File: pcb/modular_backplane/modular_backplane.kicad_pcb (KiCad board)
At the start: 2 copper layers, 63.5 x 114.3 mm, 50 parts, among them U1 DMP3028LK3-13, U2 DMP3028LK3-13, U3 PREC002SAAN-RC, U4 NTD4969NT4G, U5 PREC002SAAN-RC, U6 NTD4969NT4G

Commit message: updates
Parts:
- added R15: 10K, Resistor_SMD:R_1206_3216Metric_Pad1.42x1.75mm_HandSolder, F.Cu at (45.9, 48.4)
- added R16: 10K, Resistor_SMD:R_1206_3216Metric_Pad1.42x1.75mm_HandSolder, F.Cu at (50.9, 48.4)
- added i2cPins1: PREC002SAAN-RC, backplane:PREC002SAAN-RC, F.Cu at (40.8, 47.5)
- boardToCard1, boardToCard2, boardToCard3, boardToCard4, boardToCard5, boardToCard6, boardToCard7, boardToCard8, boardToCard9: value SSQ-104-02-T-S-RA -> SSQ-108-02-T-S-RA; footprint backplane:SSQ-104-02-T-S-RA -> backplane:SSQ-108-02-T-S-RA
- moved boardToCard9 38.4 mm to (63.5, 50.8)
- moved LipoGnd2 14.0 mm to (54.6, 120.7)
- moved lipoGnd1 14.0 mm to (24.1, 120.7)
- moved lipoIn1 14.0 mm to (8.89, 120.7)
- moved lipoIn2 14.0 mm to (39.4, 120.7)
- moved boardToCard4 13.7 mm to (0.00, 76.2)
- moved boardToCard7 13.7 mm to (63.5, 76.2)
- moved boardToCard8 13.7 mm to (63.5, 25.4)
- moved boardToCard2 13.7 mm to (0.00, 25.4)
- moved boardToCard3 13.7 mm to (0.00, 50.8)
- moved boardToCard5 13.7 mm to (0.00, 101.6)
- moved boardToCard6 13.7 mm to (63.5, 101.6)
- moved boardToCard1 8.89 mm to (12.7, 0.00)
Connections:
- boardToCard1 pad 2: +3V3 -> GND
- boardToCard1 pad 3: +5V -> +3V3
- boardToCard1 pad 4: +15V -> +5V
- boardToCard2 pad 2: +3V3 -> GND
- boardToCard2 pad 3: +5V -> +3V3
- boardToCard2 pad 4: +15V -> +5V
- boardToCard3 pad 2: +3V3 -> GND
- boardToCard3 pad 3: +5V -> +3V3
- boardToCard3 pad 4: +15V -> +5V
- boardToCard4 pad 2: +3V3 -> GND
- boardToCard4 pad 3: +5V -> +3V3
- boardToCard4 pad 4: +15V -> +5V
- boardToCard5 pad 2: +3V3 -> GND
- boardToCard5 pad 3: +5V -> +3V3
- boardToCard5 pad 4: +15V -> +5V
- boardToCard6 pad 2: +3V3 -> GND
- boardToCard6 pad 3: +5V -> +3V3
- boardToCard6 pad 4: +15V -> +5V
- boardToCard7 pad 2: +3V3 -> GND
- boardToCard7 pad 3: +5V -> +3V3
- boardToCard7 pad 4: +15V -> +5V
- boardToCard8 pad 2: +3V3 -> GND
- boardToCard8 pad 3: +5V -> +3V3
- boardToCard8 pad 4: +15V -> +5V
- boardToCard9 pad 2: +3V3 -> GND
- boardToCard9 pad 3: +5V -> +3V3
- boardToCard9 pad 4: +15V -> +5V
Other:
- board size 63.5 x 114.3 mm -> 63.5 x 127 mm

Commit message: updates
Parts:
- removed boardToCard1, boardToCard2, boardToCard3, boardToCard4, boardToCard5, boardToCard6, boardToCard7, boardToCard8, boardToCard9: SSQ-108-02-T-S-RA, backplane:SSQ-108-02-T-S-RA
- added U7: PREC027DAAN-RC, backplane:PREC027DAAN-RC, F.Cu at (29.2, 61.0)
- added card1: PPPC072LJBN-RC, backplane:PPPC072LJBN-RC, F.Cu at (12.7, 2.54)
- added card2: PPPC072LJBN-RC, backplane:PPPC072LJBN-RC, F.Cu at (2.54, 25.4)
- added card3: PPPC072LJBN-RC, backplane:PPPC072LJBN-RC, F.Cu at (2.54, 50.8)
- added card4: PPPC072LJBN-RC, backplane:PPPC072LJBN-RC, F.Cu at (2.54, 76.2)
- added card5: PPPC072LJBN-RC, backplane:PPPC072LJBN-RC, F.Cu at (2.54, 101.6)
- added card6: PPPC072LJBN-RC, backplane:PPPC072LJBN-RC, F.Cu at (61.0, 101.6)
- added card7: PPPC072LJBN-RC, backplane:PPPC072LJBN-RC, F.Cu at (61.0, 76.2)
- added card8: PPPC072LJBN-RC, backplane:PPPC072LJBN-RC, F.Cu at (61.0, 50.8)
- added card9: PPPC072LJBN-RC, backplane:PPPC072LJBN-RC, F.Cu at (61.0, 25.4)
- R15, R16: value 10K -> 4.7K
- moved barrelJack1 3.81 mm to (45.1, 5.08)
- moved barrelJack3 3.81 mm to (34.9, 5.08)
- moved barrelJack2 3.81 mm to (55.2, 5.08)

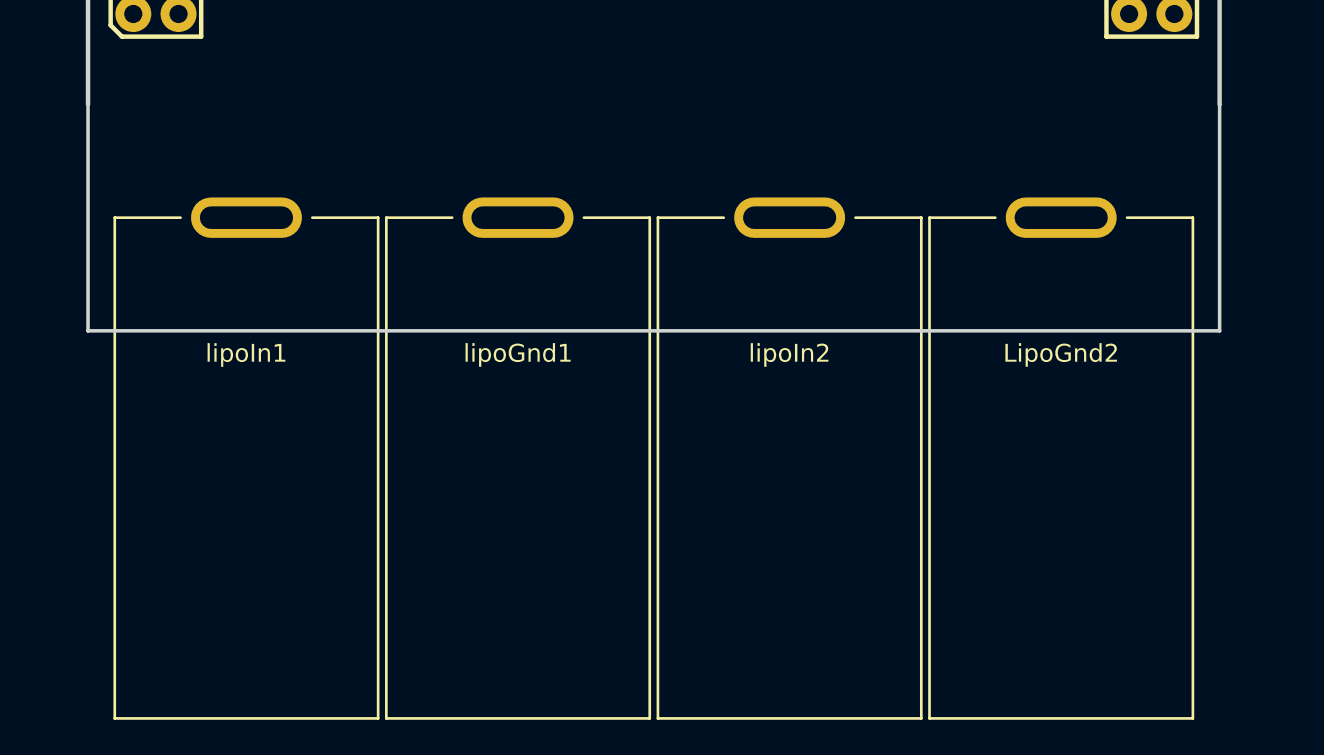
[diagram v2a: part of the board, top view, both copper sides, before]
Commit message: layers
i added plane layers to prepare for routing
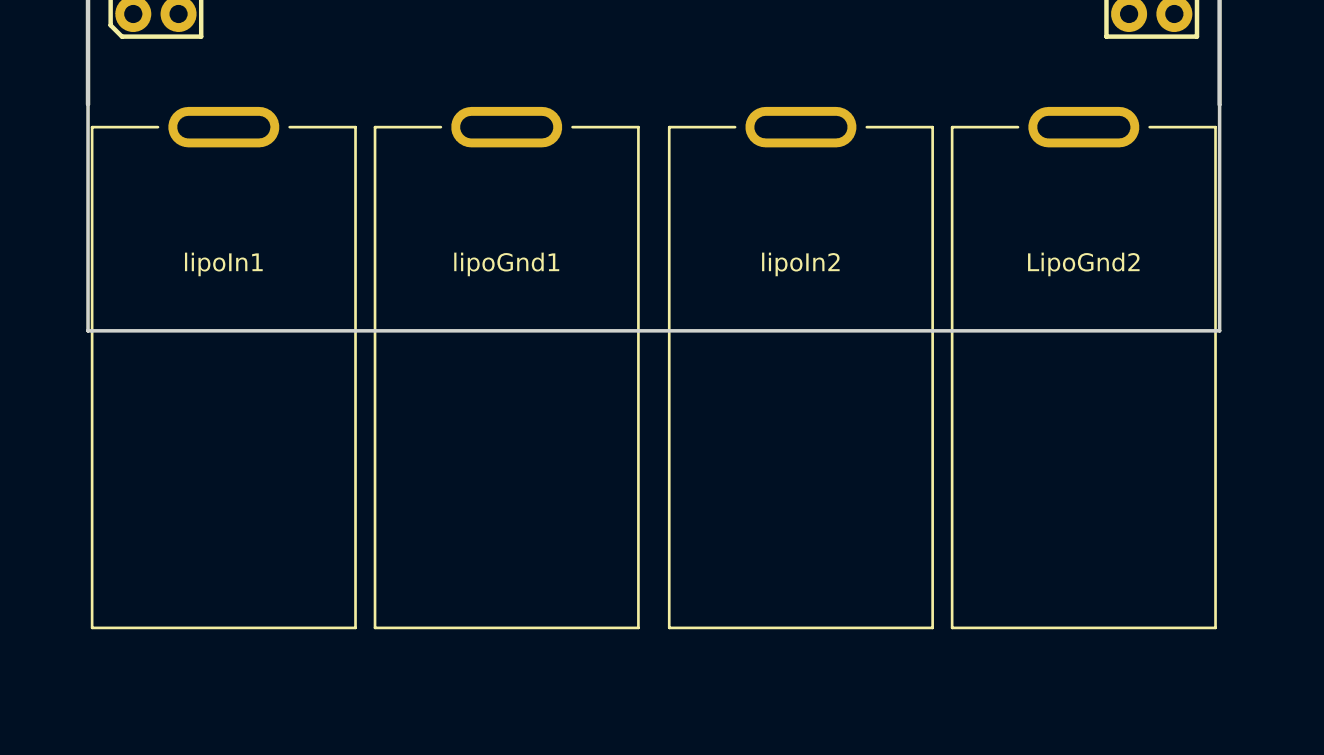
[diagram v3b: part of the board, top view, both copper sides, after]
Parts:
- L1, L2: value 15uH -> 10uH
- moved LipoGnd2 5.24 mm to (55.9, 115.6)
- moved lipoIn1 5.24 mm to (7.62, 115.6)
- moved lipoIn2 5.12 mm to (40.0, 115.6)
- moved lipoGnd1 5.12 mm to (23.5, 115.6)
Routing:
- added copper zone on PWR_PLANE, net +15V
- added copper zone on GND_PLANE, net GND
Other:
- copper layers 2 -> 4

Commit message: added 12v line
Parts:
- added C11: 22uF, backplane:865090442004, F.Cu at (-21.7, -115.5)
- added C12: 47uF, backplane:865090449007, F.Cu at (-19.8, -122.7)
- added C13: 10nF, Capacitor_SMD:C_1206_3216Metric_Pad1.42x1.75mm_HandSolder, F.Cu at (-15.5, -114.7)
- added C14: 100nF, Capacitor_SMD:C_1206_3216Metric_Pad1.42x1.75mm_HandSolder, F.Cu at (-0.57, -118.0)
- added C15: 6.8nF, Capacitor_SMD:C_1206_3216Metric_Pad1.42x1.75mm_HandSolder, F.Cu at (-10.6, -114.7)
- added L3: 15uH, backplane:6100-150K-RC, F.Cu at (47.6, 27.9)
- added R17: 120K, Resistor_SMD:R_1206_3216Metric_Pad1.42x1.75mm_HandSolder, F.Cu at (-15.5, -112.4)
- added R18: 10K, Resistor_SMD:R_1206_3216Metric_Pad1.42x1.75mm_HandSolder, F.Cu at (-10.6, -112.4)
- added R19: 6.8k, Resistor_SMD:R_1206_3216Metric_Pad1.42x1.75mm_HandSolder, F.Cu at (-0.57, -115.7)
- added R20: 100K, Resistor_SMD:R_1206_3216Metric_Pad1.42x1.75mm_HandSolder, F.Cu at (-5.62, -114.7)
- added rail12v1: AP6503SP-13, backplane:AP6503SP-13, F.Cu at (43.2, 17.8)
- L1, L2: footprint backplane:6100-150K-RC -> backplane:RCH8011NP-100L
- moved card6 76.2 mm to (61.0, 25.4)
- moved card9 76.2 mm to (61.0, 101.6)
- moved card7 25.4 mm to (61.0, 50.8)
- moved card8 25.4 mm to (61.0, 76.2)
- moved U7 13.0 mm to (31.8, 73.7), turned to 270 degrees
- moved rail5v1 10.5 mm to (27.9, 17.8)
- moved U6 8.91 mm to (43.2, 77.5)
- moved rail3v1 6.75 mm to (15.2, 17.8)
- moved barrelJack1 0.63 mm to (45.1, 5.71)
- moved barrelJack2 0.63 mm to (55.2, 5.71)
- moved barrelJack3 0.63 mm to (34.9, 5.71)
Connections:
- U7 pad 1: Net-(U7-Pad1) -> header1Gpio2
- U7 pad 10: Net-(U7-Pad10) -> header2Gpio3
- U7 pad 11: Net-(U7-Pad11) -> header2Gpio6
- U7 pad 12: Net-(U7-Pad12) -> header2Gpio5
- U7 pad 13: Net-(U7-Pad13) -> header3Gpio2
- U7 pad 14: Net-(U7-Pad14) -> header3Gpio1
- U7 pad 15: Net-(U7-Pad15) -> header3Gpio4
- U7 pad 16: Net-(U7-Pad16) -> header3Gpio3
- U7 pad 17: Net-(U7-Pad17) -> header3Gpio6
- U7 pad 18: Net-(U7-Pad18) -> header3Gpio5
- U7 pad 19: Net-(U7-Pad19) -> header4Gpio2
- U7 pad 2: Net-(U7-Pad2) -> header1Gpio1
- U7 pad 20: Net-(U7-Pad20) -> header4Gpio1
- U7 pad 21: Net-(U7-Pad21) -> header4Gpio4
- U7 pad 22: Net-(U7-Pad22) -> header4Gpio3
- U7 pad 23: Net-(U7-Pad23) -> header4Gpio6
- U7 pad 24: Net-(U7-Pad24) -> header4Gpio5
- U7 pad 25: Net-(U7-Pad25) -> header5Gpio2
- U7 pad 26: Net-(U7-Pad26) -> header5Gpio1
- U7 pad 27: Net-(U7-Pad27) -> header5Gpio4
- U7 pad 28: Net-(U7-Pad28) -> header5Gpio3
- U7 pad 29: Net-(U7-Pad29) -> header5Gpio6
- U7 pad 3: Net-(U7-Pad3) -> header1Gpio4
- U7 pad 30: Net-(U7-Pad30) -> header5Gpio5
- U7 pad 31: Net-(U7-Pad31) -> header6Gpio2
- U7 pad 32: Net-(U7-Pad32) -> header6Gpio1
- U7 pad 33: Net-(U7-Pad33) -> header6Gpio4
- U7 pad 34: Net-(U7-Pad34) -> header6Gpio3
- U7 pad 35: Net-(U7-Pad35) -> header6Gpio6
- U7 pad 36: Net-(U7-Pad36) -> header6Gpio5
- U7 pad 37: Net-(U7-Pad37) -> header7Gpio2
- U7 pad 38: Net-(U7-Pad38) -> header7Gpio1
- U7 pad 39: Net-(U7-Pad39) -> header7Gpio4
- U7 pad 4: Net-(U7-Pad4) -> header1Gpio3
- U7 pad 40: Net-(U7-Pad40) -> header7Gpio3
- U7 pad 41: Net-(U7-Pad41) -> header7Gpio6
- U7 pad 42: Net-(U7-Pad42) -> header7Gpio5
- U7 pad 43: Net-(U7-Pad43) -> header8Gpio2
- U7 pad 44: Net-(U7-Pad44) -> header8Gpio1
- U7 pad 45: Net-(U7-Pad45) -> header8Gpio4
- U7 pad 46: Net-(U7-Pad46) -> header8Gpio3
- U7 pad 47: Net-(U7-Pad47) -> header8Gpio6
- U7 pad 48: Net-(U7-Pad48) -> header8Gpio5
- U7 pad 49: Net-(U7-Pad49) -> header9Gpio2
- U7 pad 5: Net-(U7-Pad5) -> header1Gpio6
- U7 pad 50: Net-(U7-Pad50) -> header9Gpio1
- U7 pad 51: Net-(U7-Pad51) -> header9Gpio4
- U7 pad 52: Net-(U7-Pad52) -> header9Gpio3
- U7 pad 53: Net-(U7-Pad53) -> header9Gpio6
- U7 pad 54: Net-(U7-Pad54) -> header9Gpio5
- U7 pad 6: Net-(U7-Pad6) -> header1Gpio5
- U7 pad 7: Net-(U7-Pad7) -> header2Gpio2
- U7 pad 8: Net-(U7-Pad8) -> header2Gpio1
- U7 pad 9: Net-(U7-Pad9) -> header2Gpio4
- barrelJack2 pad 1: +15V -> +12V

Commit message: done
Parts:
- removed R4, R8: 10K, Resistor_SMD:R_1206_3216Metric_Pad1.42x1.75mm_HandSolder
- removed R7: 42K, Resistor_SMD:R_1206_3216Metric_Pad1.42x1.75mm_HandSolder
- removed U6: NTD4969NT4G, backplane:NTD4969NT4G
- removed U7: PREC027DAAN-RC, backplane:PREC027DAAN-RC
- removed card1: PPPC072LJBN-RC, backplane:PPPC072LJBN-RC
- C1, C11, C12, C13, C14, C2, C3, C4, C6, C7, C8, C9, R15, R16: moved to B.Cu
- L3: value 15uH -> 10uH; footprint backplane:6100-150K-RC -> backplane:RCH8011NP-100L
- U5: value PREC002SAAN-RC -> PREC024DAAN-RC; footprint backplane:PREC002SAAN-RC -> backplane:PREC024DAAN-RC
- moved R14 217.6 mm to (22.7, 28.7), turned to 270 degrees
- moved R9 215.0 mm to (33.4, 36.3), turned to 180 degrees
- moved R10 208.3 mm to (37.8, 28.6), turned to 270 degrees
- moved R2 194.1 mm to (7.62, 2.79), turned to 180 degrees
- moved U5 189.7 mm to (31.8, 76.2), turned to 270 degrees
- moved C2 185.9 mm to (31.6, 16.4), turned to 180 degrees
- moved C7 177.5 mm to (17.9, 16.4), turned to 180 degrees
- moved R11 175.2 mm to (22.9, 39.4), turned to 270 degrees
- moved R17 165.7 mm to (50.9, 39.4), turned to 270 degrees
- moved C11 165.0 mm to (41.1, 37.0), turned to 270 degrees
- moved R5 164.2 mm to (37.8, 39.3), turned to 270 degrees
- moved R18 163.6 mm to (47.0, 40.8), turned to 180 degrees
- moved C10 163.3 mm to (22.7, 33.8), turned to 270 degrees
- moved R12 161.5 mm to (18.4, 40.8), turned to 180 degrees
- moved R3 160.5 mm to (7.62, 7.62)
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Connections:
- U4 pad 3: liPo1 -> +15V
- U5 pad 1: monitor2 -> header6Gpio2
- U5 pad 2: monitorEna2 -> header2Gpio6
- card2 pad 13: GND -> sda
- card2 pad 14: GND -> scl
- card2 pad 5: scl -> GND
- card2 pad 7: sda -> GND
- card3 pad 13: GND -> sda
- card3 pad 14: GND -> scl
- card3 pad 5: scl -> GND
- card3 pad 7: sda -> GND
- card4 pad 13: GND -> sda
- card4 pad 14: GND -> scl
- card4 pad 5: scl -> GND
- card4 pad 7: sda -> GND
- card5 pad 13: GND -> sda
- card5 pad 14: GND -> scl
- card5 pad 5: scl -> GND
- card5 pad 7: sda -> GND
- card6 pad 13: GND -> sda
- card6 pad 14: GND -> scl
- card6 pad 5: scl -> GND
- card6 pad 7: sda -> GND
- card7 pad 13: GND -> sda
- card7 pad 14: GND -> scl
- card7 pad 5: scl -> GND
- card7 pad 7: sda -> GND
- card8 pad 13: GND -> sda
- card8 pad 14: GND -> scl
- card8 pad 5: scl -> GND
- card8 pad 7: sda -> GND
- card9 pad 13: GND -> sda
- card9 pad 14: GND -> scl
- card9 pad 5: scl -> GND
- card9 pad 7: sda -> GND
- lipoIn2 pad 1: lipo2 -> liPo2
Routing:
- net sda: track 0.00 -> 263.0 mm
- net scl: track 0.00 -> 228.4 mm
- net header6Gpio2: track 0.00 -> 59.9 mm
- net header6Gpio1: track 0.00 -> 54.2 mm
- net header5Gpio1: track 0.00 -> 53.0 mm, vias 0 -> 1
- net header6Gpio3: track 0.00 -> 52.6 mm
- net header5Gpio2: track 0.00 -> 49.7 mm, vias 0 -> 1
- net header6Gpio4: track 0.00 -> 48.4 mm
- net header6Gpio5: track 0.00 -> 46.4 mm
- net header6Gpio6: track 0.00 -> 45.5 mm
- net header2Gpio2: track 0.00 -> 44.9 mm
- net header7Gpio2: track 0.00 -> 41.8 mm
- net header8Gpio2: track 0.00 -> 40.2 mm
- net header2Gpio6: track 0.00 -> 40.0 mm
- net header2Gpio1: track 0.00 -> 39.9 mm
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- added copper zone on F.Cu, net +12V
- added copper zone on F.Cu, net +15V
- added copper zone on PWR_PLANE2, net +3V3
- added copper zone on PWR_PLANE3, net +5V
- added copper zone on F.Cu, net GND
- added copper zone on B.Cu, net Net-(C13-Pad1)
- added copper zone on B.Cu, net Net-(C3-Pad1)
- added copper zone on B.Cu, net Net-(C8-Pad1)
- added copper zone on F.Cu, net liPo1
- added copper zone on F.Cu, net liPo2
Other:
- copper layers 4 -> 6
- board text added: "Reaper Tech"

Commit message: motordriver finished
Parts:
- removed U3: PREC002SAAN-RC, backplane:PREC002SAAN-RC
- added LipoMonitor: PREC002SAAN-RC, backplane:PREC002SAAN-RC, F.Cu at (5.08, 6.10)
- added U6: mountingHole, backplane:mountingHole, F.Cu at (3.81, 38.1)
- added U7: mountingHole, backplane:mountingHole, F.Cu at (59.7, 38.1)
- added U8: mountingHole, backplane:mountingHole, F.Cu at (3.81, 88.9)
- added U9: mountingHole, backplane:mountingHole, F.Cu at (59.7, 88.9)
- moved R16 60.2 mm to (58.7, 64.0), turned to 0 degrees
- moved I2C 1.37 mm to (5.08, 12.6)
- moved MonitorFet 1.27 mm to (16.5, 4.45)
- moved R1 1.27 mm to (8.89, 11.4)
- moved R2 1.27 mm to (8.89, 2.79)
- moved R3 1.27 mm to (8.89, 7.62)
- moved C1 0.76 mm to (27.3, 37.1)
- moved C6 0.40 mm to (12.2, 37.3)
- renumbered card2 to Card1, card3 to Card2, card4 to Card3, card5 to Card4, card9 to Card5, card8 to Card6, card7 to Card7, card6 to Card8, U5 to CentralHub, i2cPins1 to I2C, U4 to MonitorFet, U1 to ReversePolarityFet1, U2 to ReversePolarityFet2
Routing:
- net scl: track 228.4 -> 245.1 mm
- net header7Gpio1: track 38.1 -> 36.1 mm
- net header6Gpio2: track 59.9 -> 61.4 mm
- net header9Gpio2: track 35.0 -> 33.7 mm
- net header5Gpio2: track 49.7 -> 48.4 mm
- net header6Gpio3: track 52.6 -> 51.3 mm
- net header7Gpio2: track 41.8 -> 41.1 mm
- net header4Gpio2: track 34.9 -> 34.2 mm
- net header2Gpio2: track 44.9 -> 45.5 mm
- net sda: track 263.0 -> 262.5 mm
- net GND: vias 60 -> 58
- net +15V: vias 42 -> 44

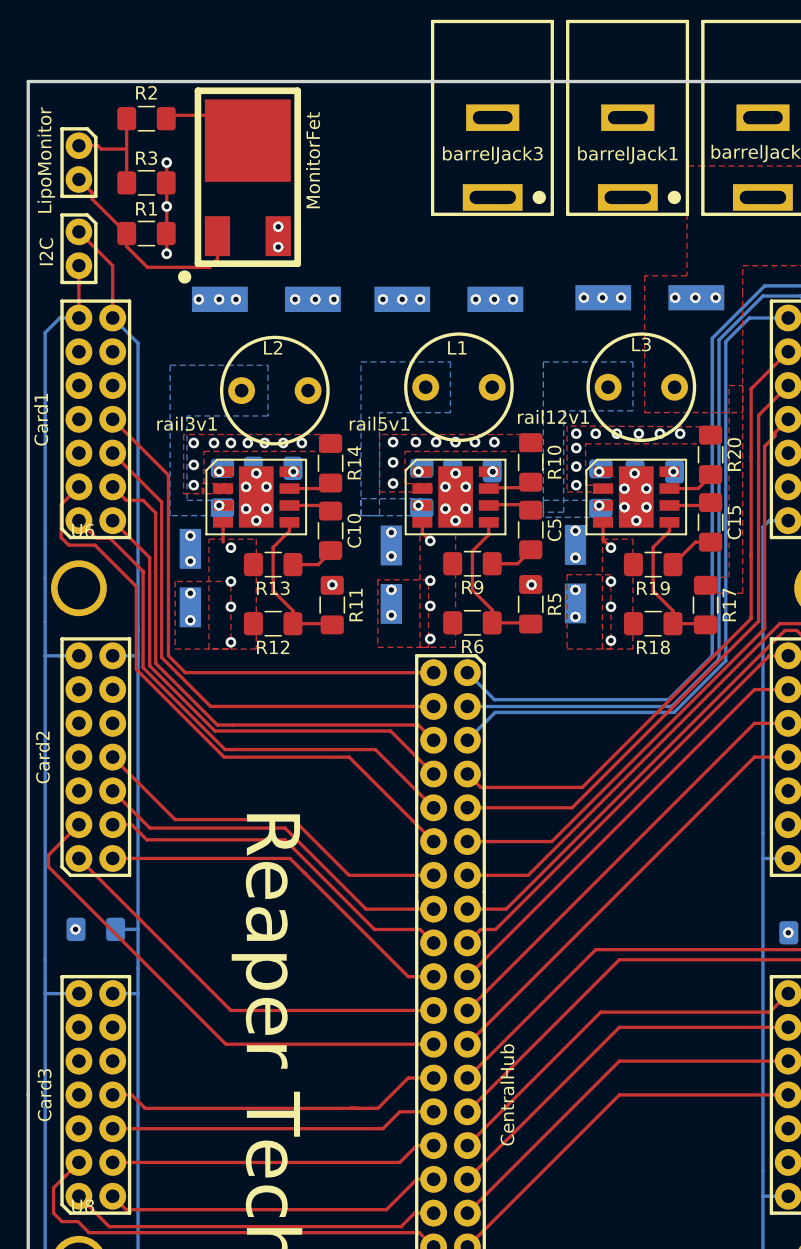
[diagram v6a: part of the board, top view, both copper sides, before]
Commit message: voltage divider
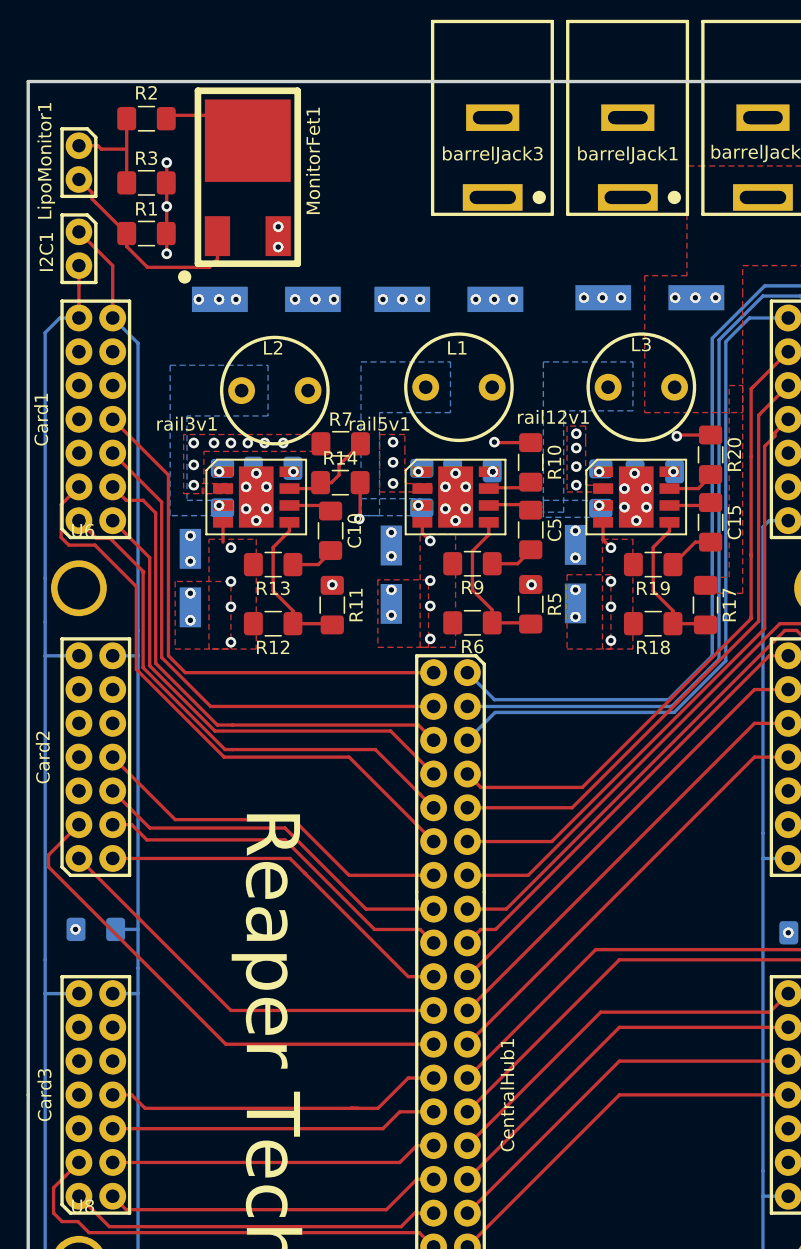
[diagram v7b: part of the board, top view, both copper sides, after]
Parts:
- added R7: 200K, Resistor_SMD:R_1206_3216Metric_Pad1.42x1.75mm_HandSolder, F.Cu at (23.5, 27.2)
- moved R14 1.64 mm to (23.5, 30.2), turned to 0 degrees
- renumbered CentralHub to CentralHub1, I2C to I2C1, LipoMonitor to LipoMonitor1, MonitorFet to MonitorFet1
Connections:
- R10 pad 1: +15V -> +3V3
- R14 pad 1: +15V -> Net-(R14-Pad1)
- R14 pad 2: Net-(R14-Pad2) -> GND
- R20 pad 1: +15V -> +3V3
- rail3v1 pad 7: Net-(R14-Pad2) -> Net-(R14-Pad1)
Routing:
- net Net-(R14-Pad1): track 0.00 -> 7.16 mm
- net +3V3: track 0.00 -> 5.32 mm, vias 6 -> 8
- net Net-(R14-Pad2): track 3.39 -> 0.00 mm
- net GND: track 12.1 -> 14.9 mm, vias 58 -> 59
- net +15V: vias 44 -> 33
